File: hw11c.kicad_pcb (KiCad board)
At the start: 2 copper layers, 49.5 x 27.5 mm, 58 parts, among them Q1 KX-7_12MHZ, SW1 BUTT1, SW2 BUTT2, X1 ~RESET, X10 PIO2.8, X11 PIO1.4, X12 PAD, X13 PIO0.8, X14 PIO0.9, X2 SWCLK, X3 SWDIO, X4 SSEL1, X5 SCK1, X6 MISO1, X7 MOSI1, X8 PIO2.6, X9 PIO2.7

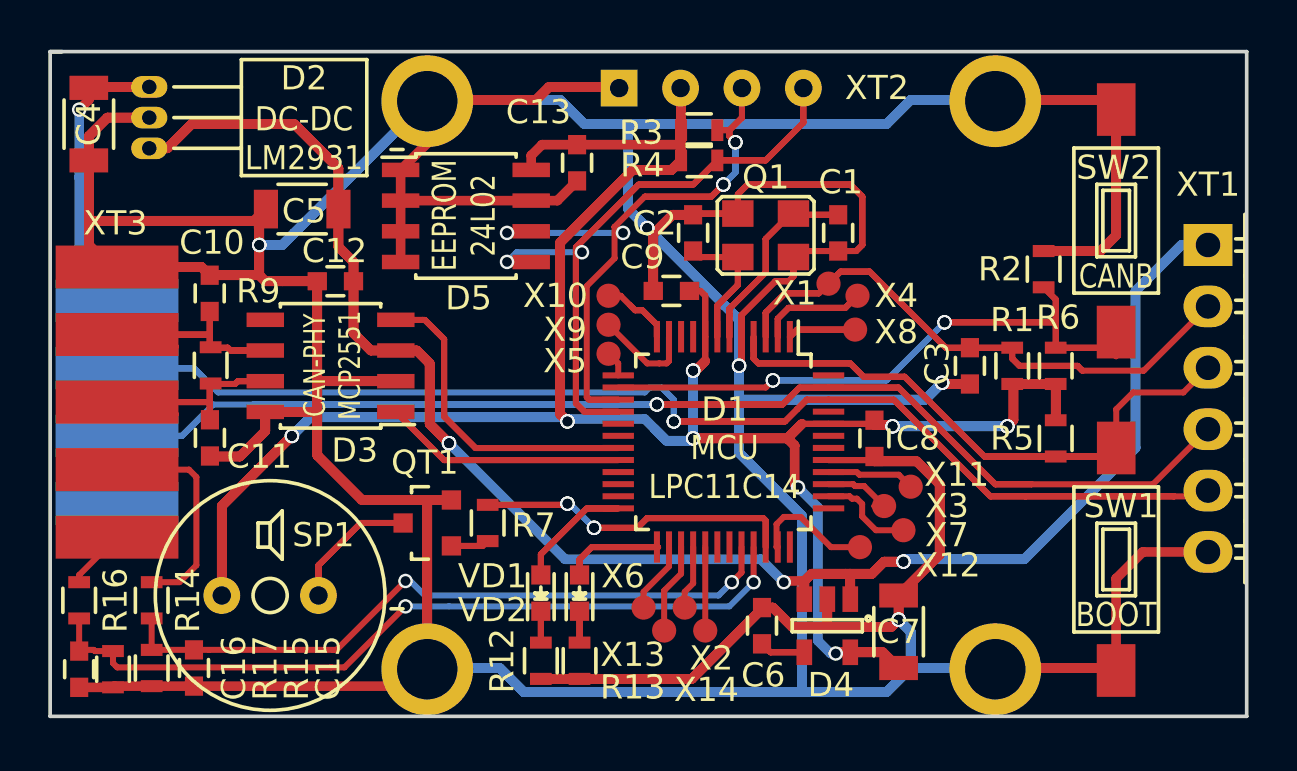
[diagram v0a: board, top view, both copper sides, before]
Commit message: Add termistor support in AN1 channel. Fix silk layer in board.
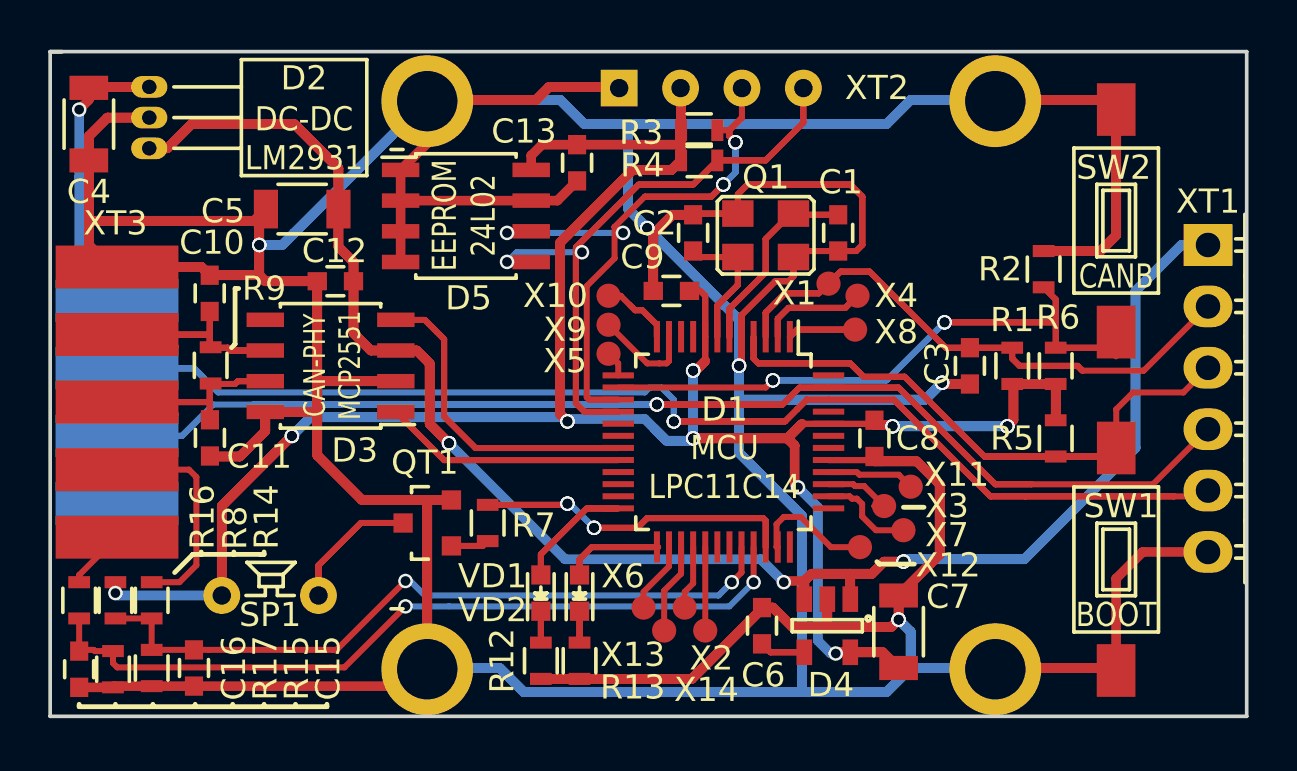
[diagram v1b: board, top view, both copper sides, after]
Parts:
- added R8: 10k, libs:R_0603, F.Cu at (52.6, 72.7)
- R14: value 10k -> 0
- R15: value 10k -> inf
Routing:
- net /3.3V: track 154.4 -> 159.3 mm, vias 14 -> 15
- net /ADC0: track 28.6 -> 30.1 mm
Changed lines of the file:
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@@
 (kicad_pcb (version 4) (host pcbnew 4.0.1-stable)
   (general
-    (links 125)
+    (links 127)
     (no_connects 0)
-    (area 49.555 49.605 109.471429 83.700001)
+    (area 49.824999 49.924999 99.475001 77.575001)
     (thickness 1.6)
-    (drawings 14)
-    (tracks 901)
+    (drawings 35)
+    (tracks 906)
     (zones 0)
-    (modules 58)
+    (modules 59)
     (nets 60)
   )
@@
     (add_net GND)
   )
+  (module libs:HC0901F (layer F.Cu)
+    (at 59 72.5)
+    (fp_text reference SP1 (at 0 0.8 180) (layer F.SilkS)
+      (effects (font (size 1 1) (thickness 0.15)))
+    )
+    (fp_text value SPEAKER (at 0 0) (layer F.Fab) hide
+      (effects (font (size 1 1) (thickness 0.15)))
+    )
+    (fp_line (start 0.3 0) (end 0.3 -0.3) (layer F.SilkS) (width 0.15))
+    (fp_line (start -0.2 0) (end -0.2 -0.3) (layer F.SilkS) (width 0.15))
+    (fp_line (start 1 0) (end 0.3 0) (layer F.SilkS) (width 0.15))
+    (fp_line (start -1 0) (end -0.2 0) (layer F.SilkS) (width 0.15))
+    (fp_line (start -0.46 -0.87) (end -0.96 -1.37) (layer F.SilkS) (width 0.15))
+    (fp_line (start -0.96 -1.37) (end 1.04 -1.37) (layer F.SilkS) (width 0.15))
+    (fp_line (start 1.04 -1.37) (end 0.54 -0.87) (layer F.SilkS) (width 0.15))
+    (fp_line (start -0.46 -0.37) (end 0.54 -0.37) (layer F.SilkS) (width 0.15))
+    (fp_line (start 0.54 -0.37) (end 0.54 -0.87) (layer F.SilkS) (width 0.15))
+    (fp_line (start 0.54 -0.87) (end -0.46 -0.87) (layer F.SilkS) (width 0.15))
+    (fp_line (start -0.46 -0.87) (end -0.46 -0.37) (layer F.SilkS) (width 0.15))
+    (pad 1 thru_hole circle (at -2 0) (size 1.524 1.524) (drill 0.762) (layers *.Cu *.Mask F.SilkS)
+      (net 7 /3.3V))
+    (pad 2 thru_hole circle (at 2 0) (size 1.524 1.524) (drill 0.762) (layers *.Cu *.Mask F.SilkS)
+      (net 45 "Net-(QT1-Pad3)"))
+  )
   (module libs:Pin_Header_Angled_1x06 locked (layer F.Cu)
     (at 97.8 58)
     (descr "Through hole pin header")
     (tags "pin header")
-    (fp_text reference XT1 (at 0 -2.5) (layer F.SilkS)
+    (fp_text reference XT1 (at 0 -1.8) (layer F.SilkS)
       (effects (font (size 1 1) (thickness 0.15)))
     )
@@
     (tags "capacitor 1206")
     (attr smd)
-    (fp_text reference C7 (at 0 0 180) (layer F.SilkS)
+    (fp_text reference C7 (at 1.45 2.05 180) (layer F.SilkS)
       (effects (font (size 1 1) (thickness 0.15)))
     )
@@
     (tags "capacitor 1206")
     (attr smd)
-    (fp_text reference C4 (at 0 0 450) (layer F.SilkS)
+    (fp_text reference C4 (at 2.8 0 540) (layer F.SilkS)
       (effects (font (size 1 1) (thickness 0.15)))
     )
@@
     (tags "capacitor 1206")
     (attr smd)
-    (fp_text reference C5 (at -0.075 -0.085 360) (layer F.SilkS)
+    (fp_text reference C5 (at 3.275 -0.085 360) (layer F.SilkS)
       (effects (font (size 1 1) (thickness 0.15)))
     )
@@
       (rotate (xyz 0 0 0))
     )
-  )
-  (module libs:HC0901F (layer F.Cu)
-    (at 59 72.5)
-    (fp_text reference SP1 (at 2.2 -2.5) (layer F.SilkS)
-      (effects (font (size 1 1) (thickness 0.15)))
-    )
-    (fp_text value SPEAKER (at 0 0) (layer F.Fab) hide
-      (effects (font (size 1 1) (thickness 0.15)))
-    )
-    (fp_line (start 0 -3) (end 0.5 -3.5) (layer F.SilkS) (width 0.15))
-    (fp_line (start 0.5 -3.5) (end 0.5 -1.5) (layer F.SilkS) (width 0.15))
-    (fp_line (start 0.5 -1.5) (end 0 -2) (layer F.SilkS) (width 0.15))
-    (fp_line (start -0.5 -3) (end -0.5 -2) (layer F.SilkS) (width 0.15))
-    (fp_line (start -0.5 -2) (end 0 -2) (layer F.SilkS) (width 0.15))
-    (fp_line (start 0 -2) (end 0 -3) (layer F.SilkS) (width 0.15))
-    (fp_line (start 0 -3) (end -0.5 -3) (layer F.SilkS) (width 0.15))
-    (fp_circle (center 0 0) (end 0.5 0.5) (layer F.SilkS) (width 0.15))
-    (fp_circle (center 0 0) (end 4.75 0) (layer F.SilkS) (width 0.15))
-    (pad 1 thru_hole circle (at -2 0) (size 1.524 1.524) (drill 0.762) (layers *.Cu *.Mask F.SilkS)
-      (net 7 /3.3V))
-    (pad 2 thru_hole circle (at 2 0) (size 1.524 1.524) (drill 0.762) (layers *.Cu *.Mask F.SilkS)
-      (net 45 "Net-(QT1-Pad3)"))
   )
   (module libs:SW_SPST_FSMSM (layer F.Cu)
@@
     (tags "capacitor 0603")
     (attr smd)
-    (fp_text reference C13 (at -2.1 1.6 360) (layer F.SilkS)
+    (fp_text reference C13 (at -1.3 2.2 360) (layer F.SilkS)
       (effects (font (size 1 1) (thickness 0.15)))
     )
@@
     (tags "resistor 0603")
     (attr smd)
-    (fp_text reference R9 (at 3.07 1.97 180) (layer F.SilkS)
+    (fp_text reference R9 (at 3.18 2.21 180) (layer F.SilkS)
       (effects (font (size 1 1) (thickness 0.15)))
     )
@@
     (tags "resistor 0603")
     (attr smd)
-    (fp_text reference R14 (at 0 1.5 270) (layer F.SilkS)
-      (effects (font (size 1 1) (thickness 0.15)))
-    )
-    (fp_text value 10k (at 0 0 90) (layer F.Fab) hide
+    (fp_text reference R14 (at 3.45 4.75 270) (layer F.SilkS)
+      (effects (font (size 1 1) (thickness 0.15)))
+    )
+    (fp_text value 0 (at 0 0 90) (layer F.Fab) hide
       (effects (font (size 1 1) (thickness 0.15)))
     )
@@
       (effects (font (size 1 1) (thickness 0.15)))
     )
-    (fp_text value 10k (at 0 1.9 270) (layer F.Fab) hide
+    (fp_text value inf (at 0 1.9 270) (layer F.Fab) hide
       (effects (font (size 1 1) (thickness 0.15)))
     )
@@
     (tags "resistor 0603")
     (attr smd)
-    (fp_text reference R16 (at 0 1.5 270) (layer F.SilkS)
+    (fp_text reference R16 (at 3.45 5.1 270) (layer F.SilkS)
       (effects (font (size 1 1) (thickness 0.15)))
     )
@@
       (net 56 /ADC3))
   )
+  (module libs:R_0603 (layer F.Cu)
+    (at 52.6 72.7 90)
+    (descr "Resistor SMD 0603, reflow soldering, Vishay (see dcrcw.pdf)")
+    (tags "resistor 0603")
+    (attr smd)
+    (fp_text reference R8 (at 3 4.95 90) (layer F.SilkS)
+      (effects (font (size 1 1) (thickness 0.15)))
+    )
+    (fp_text value 10k (at 0 0 90) (layer F.Fab) hide
+      (effects (font (size 1 1) (thickness 0.15)))
+    )
+    (fp_line (start -1.3 -0.8) (end 1.3 -0.8) (layer F.CrtYd) (width 0.05))
+    (fp_line (start -1.3 0.8) (end 1.3 0.8) (layer F.CrtYd) (width 0.05))
+    (fp_line (start -1.3 -0.8) (end -1.3 0.8) (layer F.CrtYd) (width 0.05))
+    (fp_line (start 1.3 -0.8) (end 1.3 0.8) (layer F.CrtYd) (width 0.05))
+    (fp_line (start 0.5 0.675) (end -0.5 0.675) (layer F.SilkS) (width 0.15))
+    (fp_line (start -0.5 -0.675) (end 0.5 -0.675) (layer F.SilkS) (width 0.15))
+    (pad 1 smd rect (at -0.75 0 90) (size 0.5 0.9) (layers F.Cu F.Paste F.Mask)
+      (net 54 /ADC0))
+    (pad 2 smd rect (at 0.75 0 90) (size 0.5 0.9) (layers F.Cu F.Paste F.Mask)
+      (net 7 /3.3V))
+    (model Resistors_SMD.3dshapes/R_0603.wrl
+      (at (xyz 0 0 0))
+      (scale (xyz 1 1 1))
+      (rotate (xyz 0 0 0))
+    )
+  )
+  (gr_line (start 86.05 68.85) (end 85.2 68.85) (angle 90) (layer F.SilkS) (width 0.2))
+  (gr_line (start 84.2 71.2) (end 84.1 71.1) (angle 90) (layer F.SilkS) (width 0.2))
+  (gr_line (start 85.65 71.2) (end 84.2 71.2) (angle 90) (layer F.SilkS) (width 0.2))
+  (gr_line (start 60.05 77.1) (end 60.05 77) (angle 90) (layer F.SilkS) (width 0.2))
+  (gr_line (start 58.75 77.1) (end 58.75 77) (angle 90) (layer F.SilkS) (width 0.2))
+  (gr_line (start 57.45 77.1) (end 57.45 77) (angle 90) (layer F.SilkS) (width 0.2))
+  (gr_line (start 55.9 77.1) (end 55.9 77) (angle 90) (layer F.SilkS) (width 0.2))
+  (gr_line (start 54.15 77.1) (end 54.15 77) (angle 90) (layer F.SilkS) (width 0.2))
+  (gr_line (start 52.6 77.05) (end 52.6 77) (angle 90) (layer F.SilkS) (width 0.2))
+  (gr_line (start 51.1 77.1) (end 51.1 77) (angle 90) (layer F.SilkS) (width 0.2))
+  (gr_line (start 61.35 77.1) (end 61.35 77) (angle 90) (layer F.SilkS) (width 0.2))
+  (gr_line (start 51.1 77.1) (end 61.35 77.1) (angle 90) (layer F.SilkS) (width 0.2))
+  (gr_line (start 56.15 70.8) (end 56.15 70.7) (angle 90) (layer F.SilkS) (width 0.2))
+  (gr_line (start 57.5 70.8) (end 57.5 70.7) (angle 90) (layer F.SilkS) (width 0.2))
+  (gr_line (start 58.75 70.8) (end 58.75 70.7) (angle 90) (layer F.SilkS) (width 0.2))
+  (gr_line (start 58.6 70.8) (end 58.75 70.8) (angle 90) (layer F.SilkS) (width 0.2))
+  (gr_line (start 55.8 70.8) (end 58.6 70.8) (angle 90) (layer F.SilkS) (width 0.2))
+  (gr_line (start 55.05 71.55) (end 55.8 70.8) (angle 90) (layer F.SilkS) (width 0.2))
+  (gr_line (start 57.55 59.8) (end 57.7 59.8) (angle 90) (layer F.SilkS) (width 0.2))
+  (gr_line (start 57.55 62.1) (end 57.4 62.25) (angle 90) (layer F.SilkS) (width 0.2))
+  (gr_line (start 57.55 59.8) (end 57.55 62.1) (angle 90) (layer F.SilkS) (width 0.2))
   (dimension 27.5 (width 0.3) (layer Dwgs.User)
     (gr_text "27,500 мм" (at 103.25 63.75 90) (layer Dwgs.User)
@@
   (segment (start 81.1 74.85) (end 79.7 74.85) (width 0.25) (layer F.Cu) (net 6))
   (segment (start 79.7 74.85) (end 79.35 74.5) (width 0.25) (layer F.Cu) (net 6))
+  (segment (start 52.6 71.95) (end 52.6 72.4) (width 0.4) (layer F.Cu) (net 7))
+  (segment (start 52.7 72.5) (end 57 72.5) (width 0.4) (layer B.Cu) (net 7))
+  (segment (start 52.6 72.4) (end 52.7 72.5) (width 0.4) (layer B.Cu) (net 7))
+  (via (at 52.6 72.4) (size 0.6) (drill 0.4) (layers F.Cu B.Cu) (net 7))
   (segment (start 74.9 65.6) (end 74.5 65.2) (width 0.4) (layer B.Cu) (net 7))
   (segment (start 71.4 65.2) (end 71.3 65.3) (width 0.4) (layer B.Cu) (net 7))
@@
   (segment (start 83.0727 68.4944) (end 83.2759 68.4944) (width 0.25) (layer F.Cu) (net 52))
   (segment (start 82.9732 68.3949) (end 83.0727 68.4944) (width 0.25) (layer F.Cu) (net 52))
+  (segment (start 52.6 73.45) (end 54.1 73.45) (width 0.25) (layer F.Cu) (net 54))
   (segment (start 64.6 71.9) (end 64.800002 71.9) (width 0.25) (layer B.Cu) (net 54))
   (segment (start 55.85 74.75) (end 56.475 74.75) (width 0.25) (layer F.Cu) (net 54))

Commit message: Add AN3 channel on board.
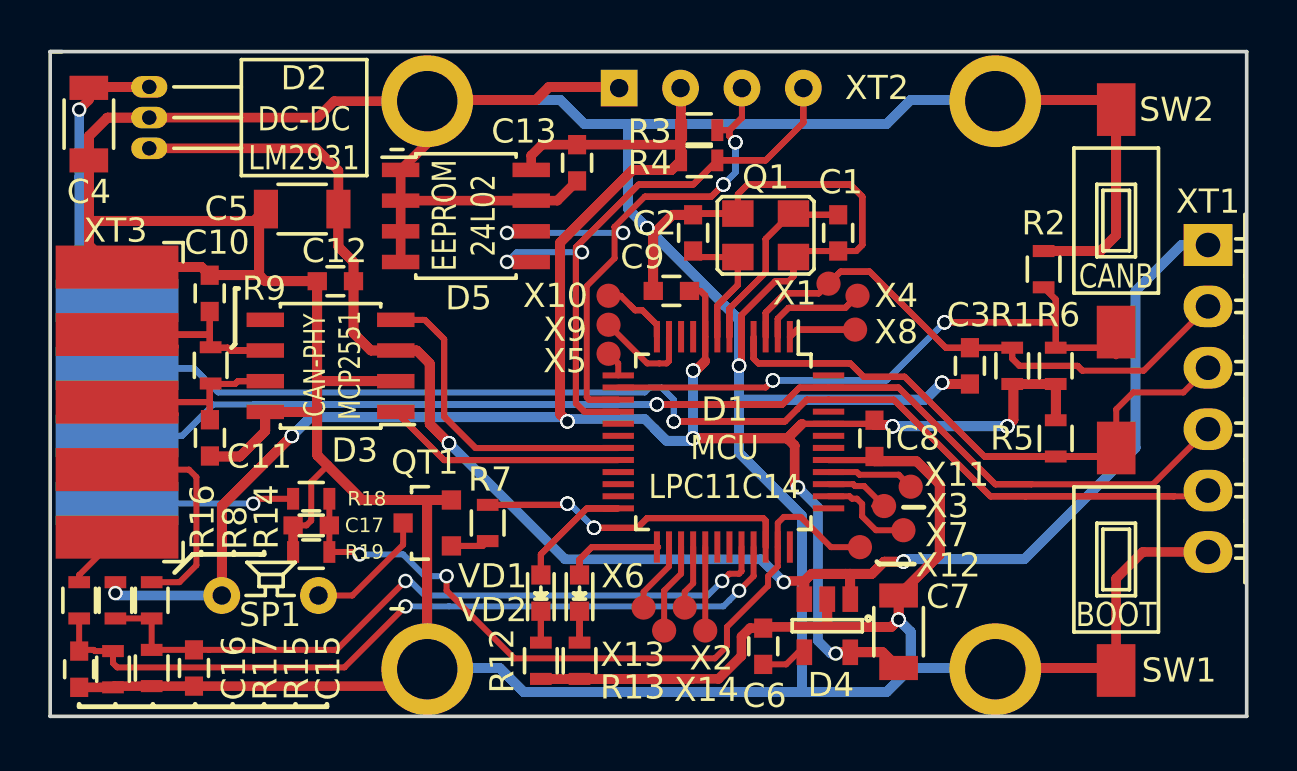
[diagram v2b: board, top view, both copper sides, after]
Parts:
- added C17: 0.1, libs:C_0603, F.Cu at (60.7, 69.6)
- added R18: 10k, libs:R_0603, F.Cu at (60.7, 68.5)
- added R19: 10k, libs:R_0603, F.Cu at (60.7, 70.7)
- moved C6 0.85 mm to (79.4, 74.6)
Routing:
- net /ADC3: track 5.09 -> 31.0 mm, vias 0 -> 2
- net /5V: track 118.9 -> 107.3 mm
- net GND: track 504.3 -> 495.6 mm, vias 10 -> 8
- net /AN3: track 0.00 -> 7.37 mm, vias 0 -> 1
- net Net-(QT1-Pad3): track 11.0 -> 5.27 mm
- net Net-(C6-Pad2): track 3.79 -> 1.91 mm

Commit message: Add connector for external buttons.
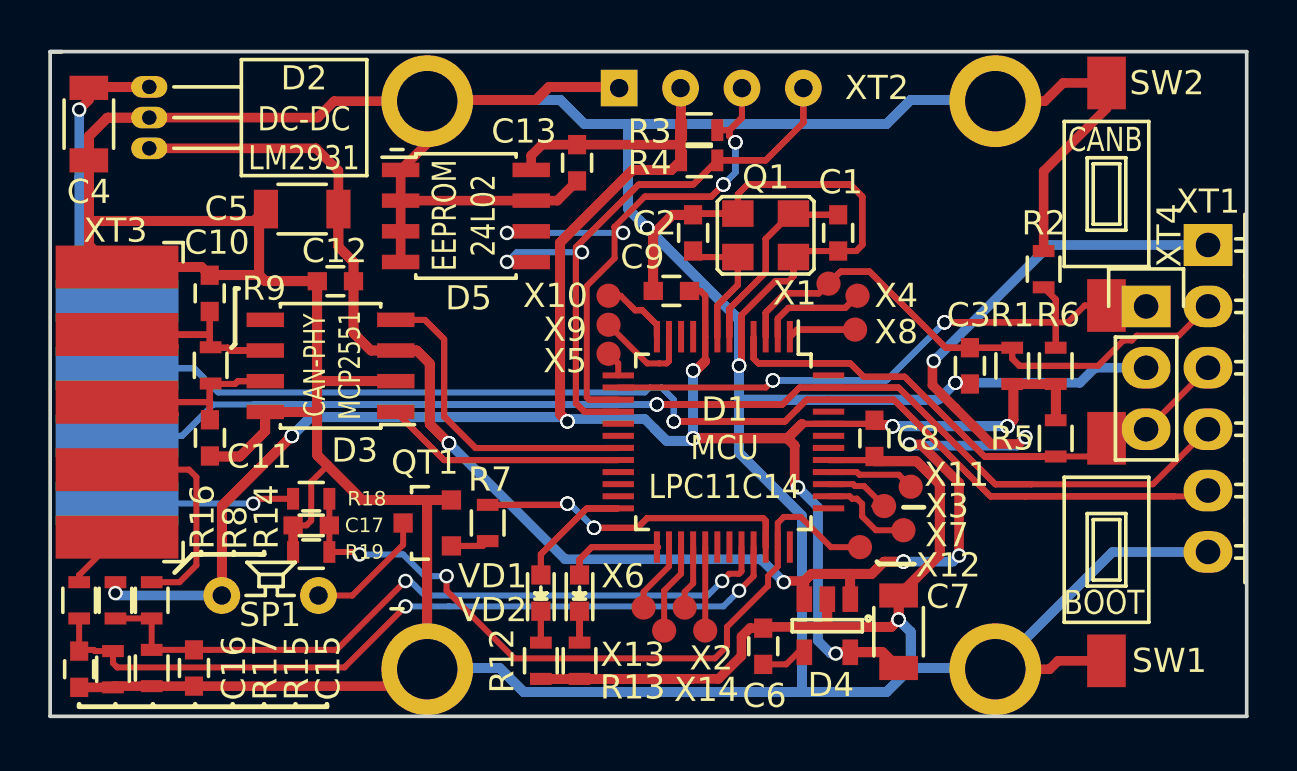
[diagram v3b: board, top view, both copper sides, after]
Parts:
- added XT4: EBUTTON, libs:Pin_Header_Straight_1x03, F.Cu at (95.2, 60.5)
- moved SW2 1.17 mm to (93.6, 55.9)
- moved SW1 0.57 mm to (93.6, 70.6)
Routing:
- net /5V: track 107.3 -> 97.2 mm, vias 5 -> 9
- net GND: track 495.6 -> 487.4 mm
- net /BOOT: track 41.6 -> 38.0 mm
- net /BUTT2: track 43.9 -> 41.4 mm

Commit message: Replace XT4 to XT5, more pins in connector (P3.0 and P3.1 to extern).
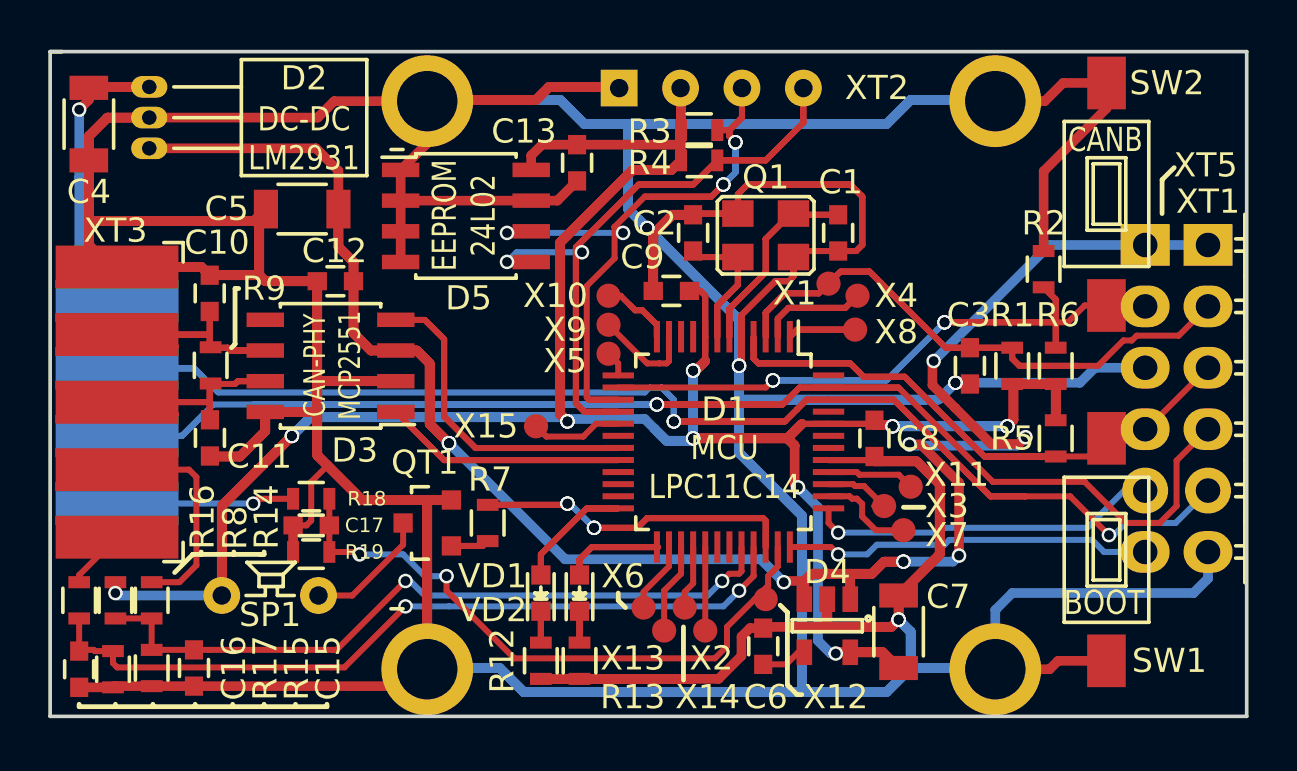
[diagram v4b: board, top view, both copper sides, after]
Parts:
- removed XT4: EBUTTON, libs:Pin_Header_Straight_1x03
- added X15: MAT0, libs:PAD, F.Cu at (70.0, 65.5)
- added XT5: EXT, libs:Pin_Header_Straight_1x06, F.Cu at (95.2, 58.0)
- X12: value PAD -> ADC3
- moved X12 4.45 mm to (79.5, 72.7)
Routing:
- net Net-(D1-Pad37): track 0.00 -> 15.4 mm, vias 0 -> 1
- net Net-(D1-Pad36): track 0.00 -> 15.3 mm, vias 0 -> 1
- net /RXD: track 76.9 -> 72.1 mm, vias 2 -> 3
- net /TXD: track 86.9 -> 82.1 mm
- net /ADC3: track 31.0 -> 27.0 mm
- net Net-(D1-Pad17): track 0.00 -> 3.80 mm
- net GND: track 487.4 -> 489.5 mm
- net /BOOT: track 38.0 -> 38.5 mm
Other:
- board text added: "igorkov / BCOMP11 igorkov.org/bcomp11v2 2018 / version 2.0"
- board text removed: "igorkov / BCOMP11 igorkov.org/bcomp11 2017 / version 2.0"
